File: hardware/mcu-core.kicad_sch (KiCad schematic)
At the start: 17 parts, among them SW1 B3U-1000P, U1 STM32F103C8T6, Y1 12MHz

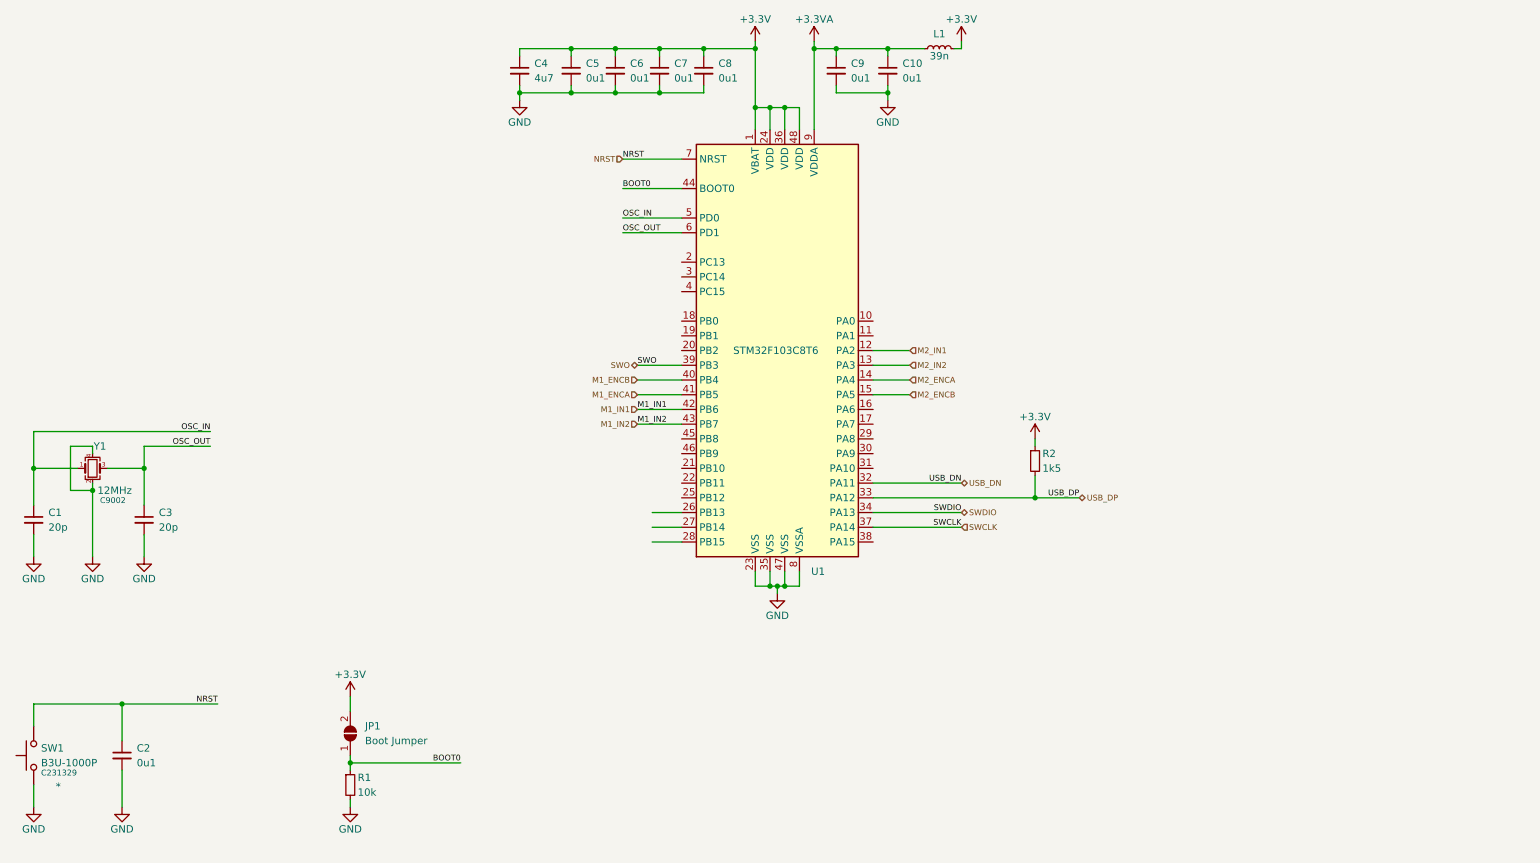
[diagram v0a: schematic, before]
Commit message: Moved hardware to separate directory
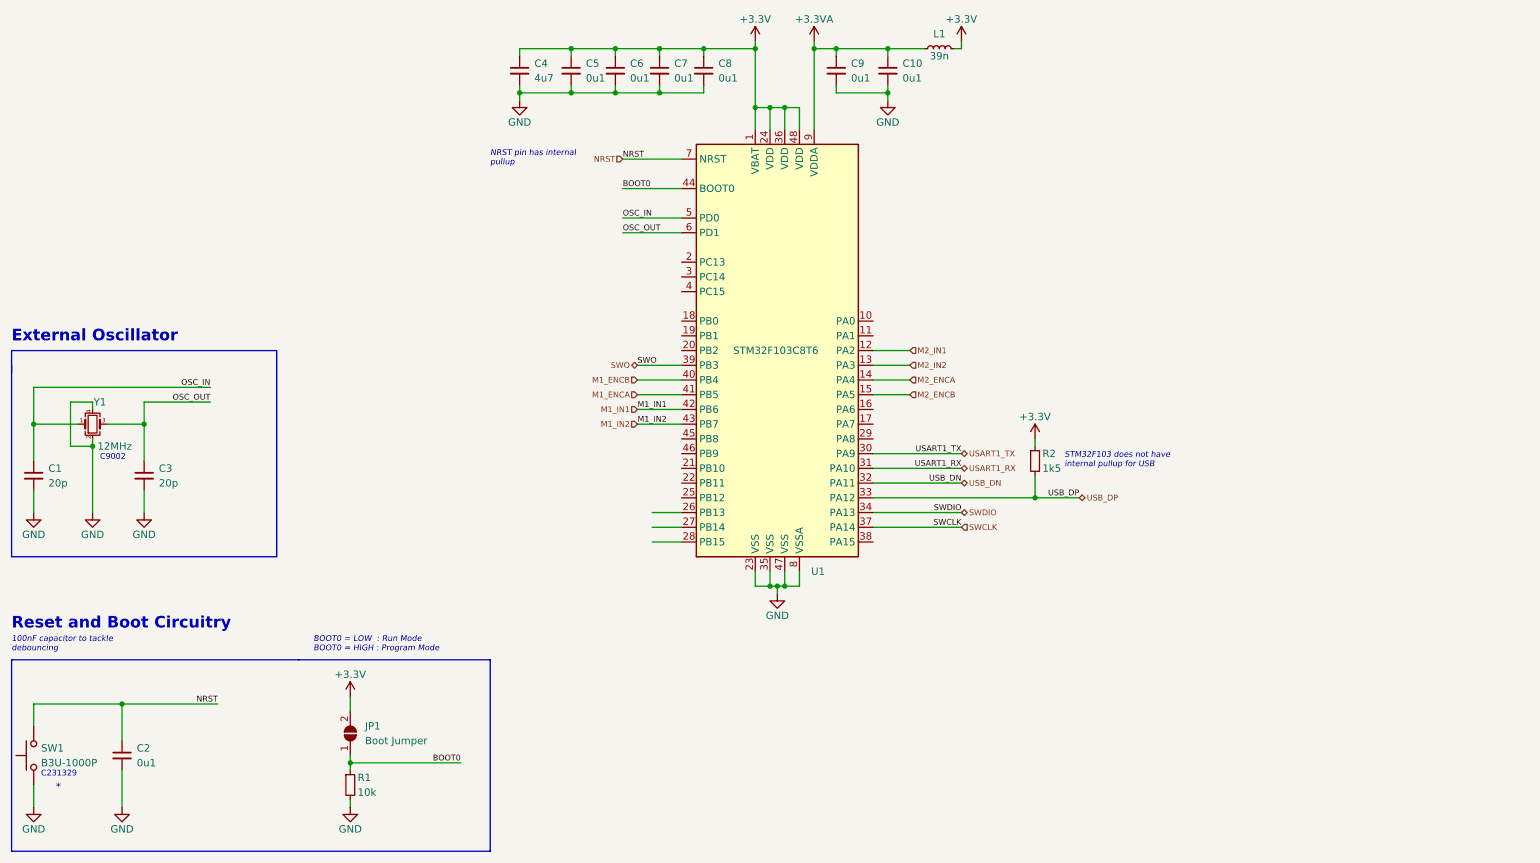
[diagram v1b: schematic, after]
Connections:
- net USART1_TX: now reaches U1.30 (PA9)
- net USART1_RX: now reaches U1.31 (PA10)
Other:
- note added: "100nF capacitor to tackle debouncing"
- note added: "BOOT0 = LOW : Run Mode BOOT0 = HIGH : Program Mode"
- note added: "External Oscillator"
- note added: "NRST pin has internal pullup"
- note added: "Reset and Boot Circuitry"
- note added: "STM32F103 does not have internal pullup for USB"
- company: (none) -> Sampreet SARKAR
- moved on the sheet: C1, C3, Y1

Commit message: Added pin assignments in firmware
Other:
- title: (none) -> Posit: A STM32 based DC motor controller
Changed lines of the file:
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@@
   (paper "A4")
   (title_block
+    (title "Posit: A STM32 based DC motor controller")
     (rev "A")
     (company "Sampreet SARKAR")

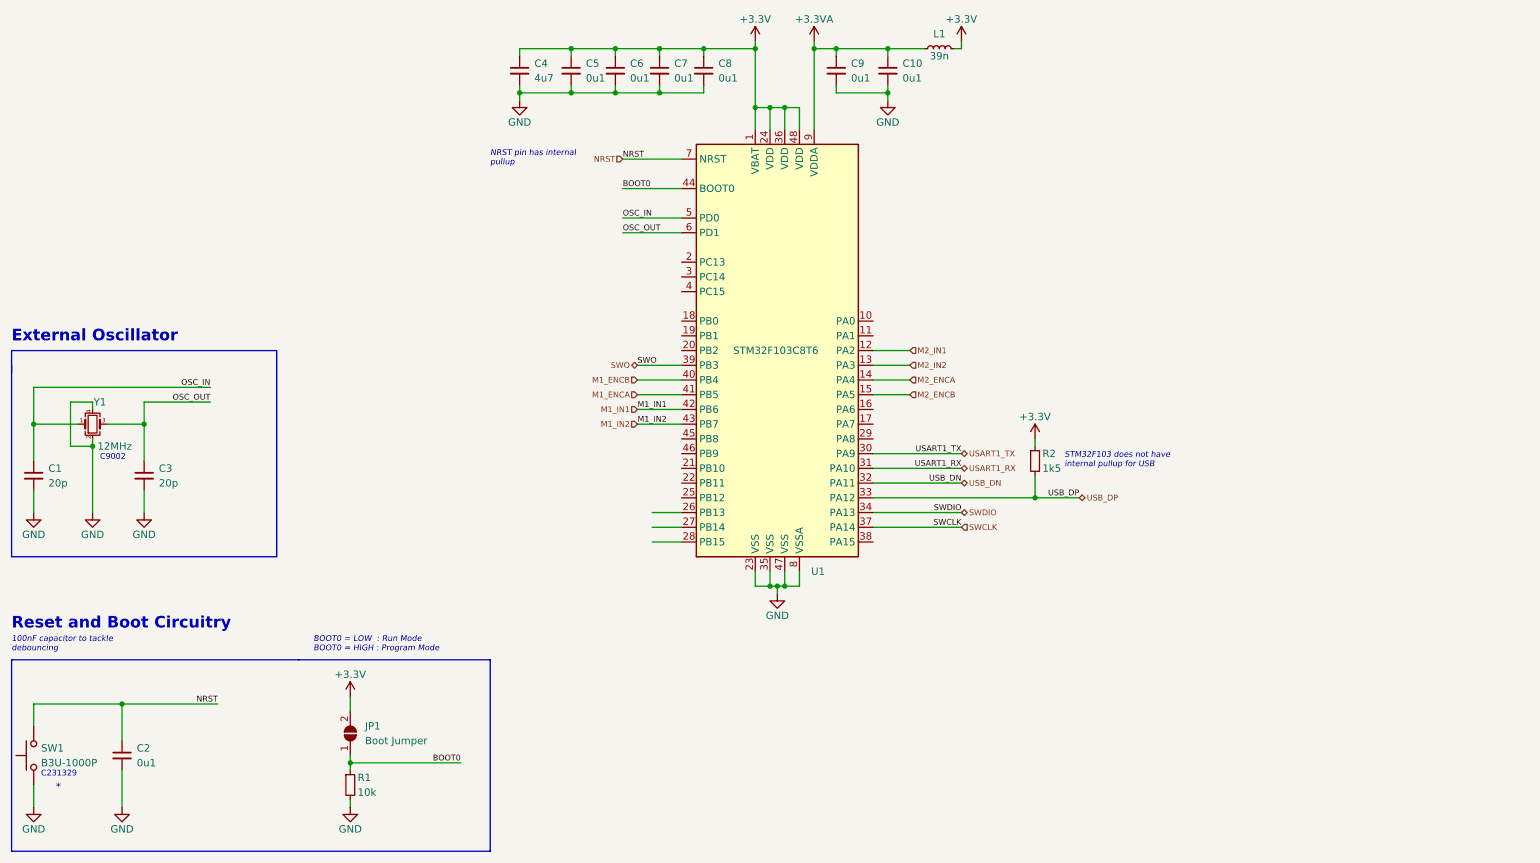
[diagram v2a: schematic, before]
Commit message: Added LEDs and UART
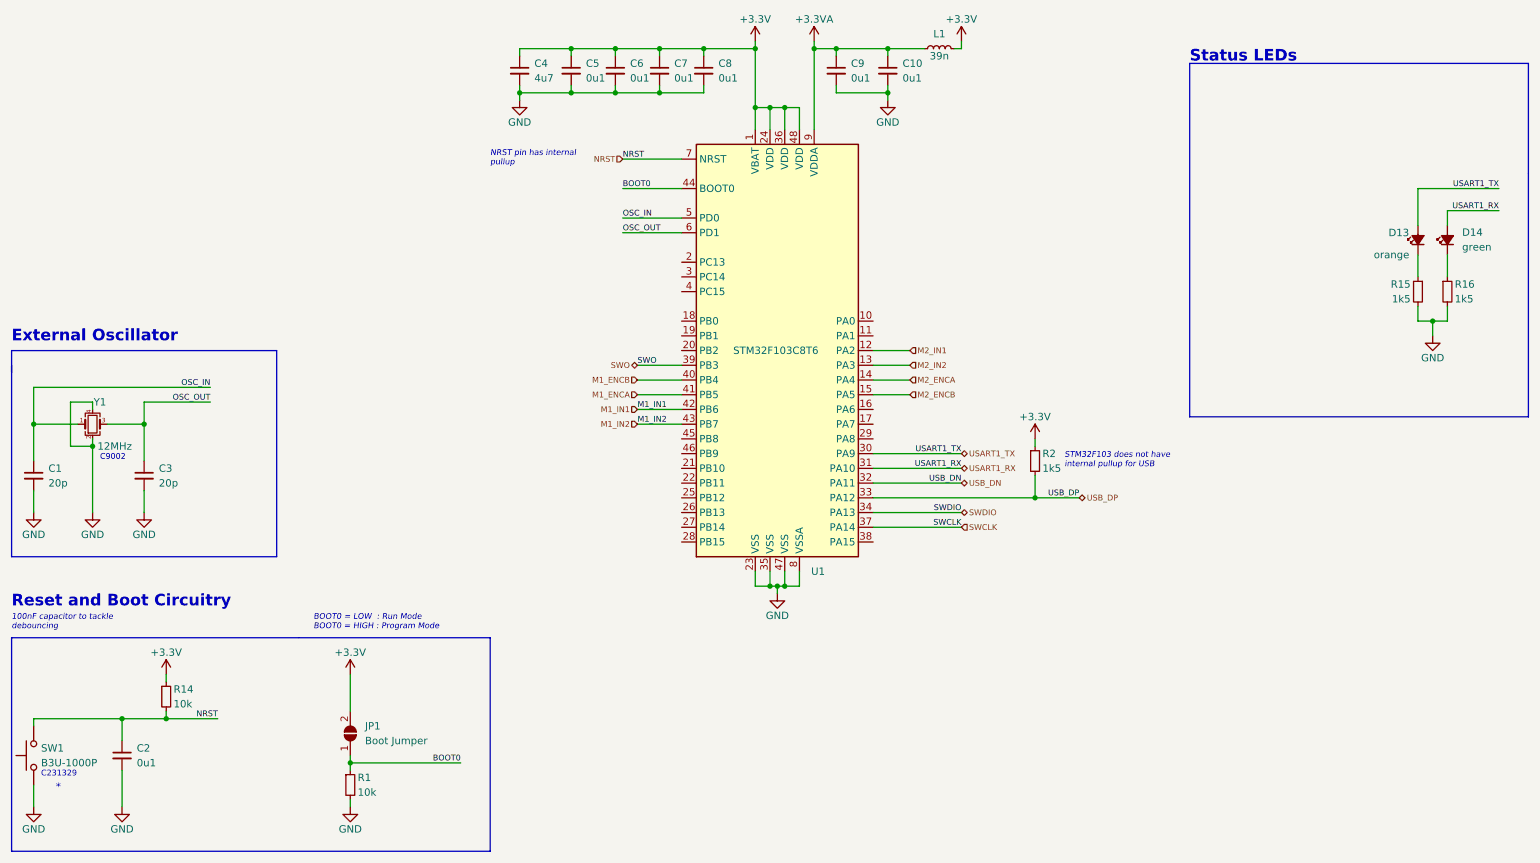
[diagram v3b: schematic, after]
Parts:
- added D13: orange, LED_SMD:LED_0603_1608Metric, symbol Device:LED_Small_Filled
- added D14: green, LED_SMD:LED_0603_1608Metric, symbol Device:LED_Small_Filled
- added R14: 10k, Resistor_SMD:R_0402_1005Metric, symbol Device:R_Small
- added R15, R16: 1k5, Resistor_SMD:R_0402_1005Metric, symbol Device:R_Small
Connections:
- net +3.3V: now also R14.1
- net GND: now also R15.2, R16.2
- net NRST: now also R14.2
- net USART1_RX: now also D14.2 (A)
- net USART1_TX: now also D13.2 (A)
- new net: D14.1 (K), R16.1
- new net: D13.1 (K), R15.1
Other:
- note added: "Status LEDs"
